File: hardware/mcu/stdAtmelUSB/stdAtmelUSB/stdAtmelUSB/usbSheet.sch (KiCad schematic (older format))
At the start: 7 parts, among them J5 Conn_01x06_Male, U8 ATSAMD11D14A-SS, X1 USBFCI_10103594_MILL

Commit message: std boards skeletons
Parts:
- added C1: 0.1uF, Capacitor_SMD:C_0402_1005Metric, symbol Device:C
- added R1: 10kOhm, Resistor_SMD:R_0402_1005Metric, symbol Device:R
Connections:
- net +3V3: now also R1.1
- net GND: now also C1.2
- net swd_rst: now also C1.1, R1.2
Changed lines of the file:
@@
 Wire Wire Line
 	6450 1550 6600 1550
+Text GLabel 1050 3150 0    50   Input ~ 0
+swd_rst
+$Comp
+L Device:C C1
+U 1 1 5E9E0263
+P 1300 3500
+F 0 "C1" H 1415 3546 50  0000 L CNN
+F 1 "0.1uF" H 1415 3455 50  0000 L CNN
+F 2 "Capacitor_SMD:C_0402_1005Metric" H 1338 3350 50  0001 C CNN
+F 3 "~" H 1300 3500 50  0001 C CNN
+	1    1300 3500
+	1    0    0    -1
+$EndComp
+$Comp
+L Device:R R1
+U 1 1 5E9E0585
+P 1300 2650
+F 0 "R1" H 1370 2696 50  0000 L CNN
+F 1 "10kOhm" H 1370 2605 50  0000 L CNN
+F 2 "Resistor_SMD:R_0402_1005Metric" V 1230 2650 50  0001 C CNN
+F 3 "~" H 1300 2650 50  0001 C CNN
+	1    1300 2650
+	1    0    0    -1
+$EndComp
+$Comp
+L power:+3V3 #PWR01
+U 1 1 5E9E1993
+P 1300 2300
+F 0 "#PWR01" H 1300 2150 50  0001 C CNN
+F 1 "+3V3" H 1315 2473 50  0000 C CNN
+F 2 "" H 1300 2300 50  0001 C CNN
+F 3 "" H 1300 2300 50  0001 C CNN
+	1    1300 2300
+	1    0    0    -1
+$EndComp
+$Comp
+L power:GND #PWR02
+U 1 1 5E9E3436
+P 1300 3900
+F 0 "#PWR02" H 1300 3650 50  0001 C CNN
+F 1 "GND" H 1305 3727 50  0000 C CNN
+F 2 "" H 1300 3900 50  0001 C CNN
+F 3 "" H 1300 3900 50  0001 C CNN
+	1    1300 3900
+	1    0    0    -1
+$EndComp
+Wire Wire Line
+	1300 3900 1300 3650
+Wire Wire Line
+	1300 2300 1300 2500
+Wire Wire Line
+	1300 2800 1300 3150
+Wire Wire Line
+	1300 3150 1050 3150
+Wire Wire Line
+	1300 3150 1300 3350
+Connection ~ 1300 3150
 $EndSCHEMATC

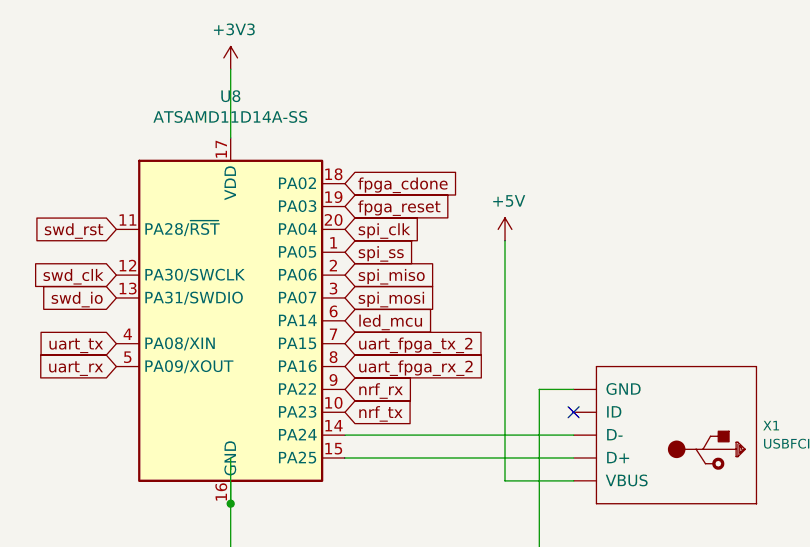
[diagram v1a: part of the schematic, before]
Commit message: u-blox GPS CAM-M8Q
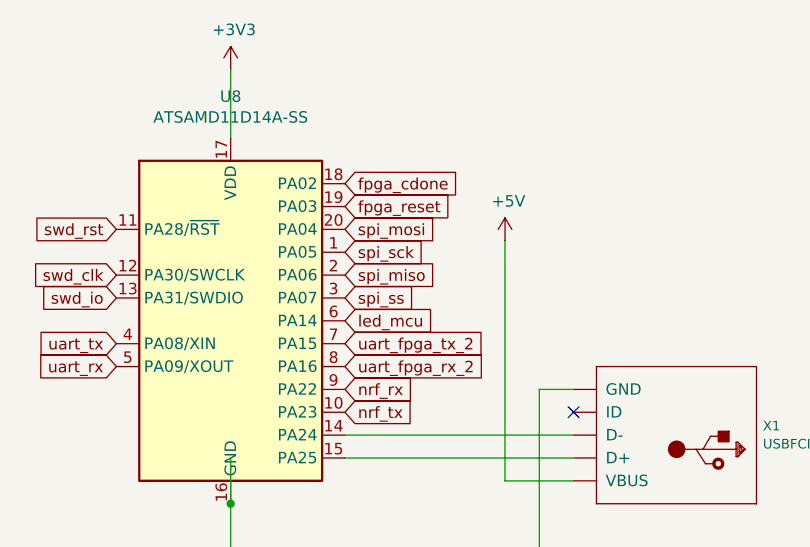
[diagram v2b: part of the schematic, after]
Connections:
- net spi_clk is gone; now on net spi_mosi: U8.20 (PA04)
- net spi_mosi: no longer U8.3 (PA07)
- net spi_ss: now also U8.3 (PA07); no longer U8.1 (PA05)
- new net spi_sck: U8.1 (PA05)
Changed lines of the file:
@@
 swd_io
 Text GLabel 3500 1800 2    50   Input ~ 0
-spi_clk
+spi_mosi
 Text GLabel 3500 1900 2    50   Input ~ 0
-spi_ss
+spi_sck
 Text GLabel 3500 2000 2    50   Input ~ 0
 spi_miso
 Text GLabel 3500 2100 2    50   Input ~ 0
-spi_mosi
+spi_ss
 Text GLabel 3500 2200 2    50   Input ~ 0
 led_mcu
